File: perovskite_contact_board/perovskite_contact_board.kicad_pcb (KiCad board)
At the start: 4 copper layers, 57 x 52.2 mm, 15 parts, among them J1 Conn_2x3, J2 Conn_2x3, J3 Conn_2x3, J4 Conn_2x3, J5 Conn2x3, J6 Conn_2x3, U1 Perovskite_CP_6_Cell, U2 Perovskite_CP_6_Cell, U3 Perovskite_CP_6_Cell, U4 MCP9808_MSOP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

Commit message: pushing changes from Monday meeting
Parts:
- U4, U5, U6: moved to B.Cu
- moved U4 2.75 mm to (184.6, 81.7)
- moved R4 0.20 mm to (199.6, 78.0)
- turned U5 to 180 degrees
- turned U6 to 180 degrees
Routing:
- net CP: track 184.7 -> 0.00 mm, vias 3 -> 0
- net Vdd: track 116.8 -> 0.00 mm, vias 4 -> 0
- net GND: track 115.5 -> 0.00 mm, vias 3 -> 0
- net SCL: track 95.3 -> 0.30 mm
- net SDA: track 86.4 -> 0.00 mm, vias 4 -> 0
- net 16: track 35.4 -> 0.00 mm, vias 1 -> 0
- net 17: track 24.7 -> 0.00 mm, vias 1 -> 0
- net 18: track 23.8 -> 0.00 mm, vias 1 -> 0
- net 4: track 22.7 -> 0.00 mm, vias 1 -> 0
- net 7: track 22.6 -> 0.00 mm, vias 1 -> 0
- net 2: track 22.4 -> 0.00 mm, vias 1 -> 0
- net 5: track 22.2 -> 0.00 mm, vias 2 -> 0
- net 3: track 21.3 -> 0.00 mm, vias 1 -> 0
- net 12: track 20.2 -> 0.00 mm, vias 1 -> 0
- net 10: track 19.0 -> 0.00 mm, vias 1 -> 0
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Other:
- copper layers 4 -> 2
- rule trace_min: 0.2 -> 0.1524
- rule via_min_drill: 0.3 -> 0.254
- rule via_min_size: 0.4 -> 0.508

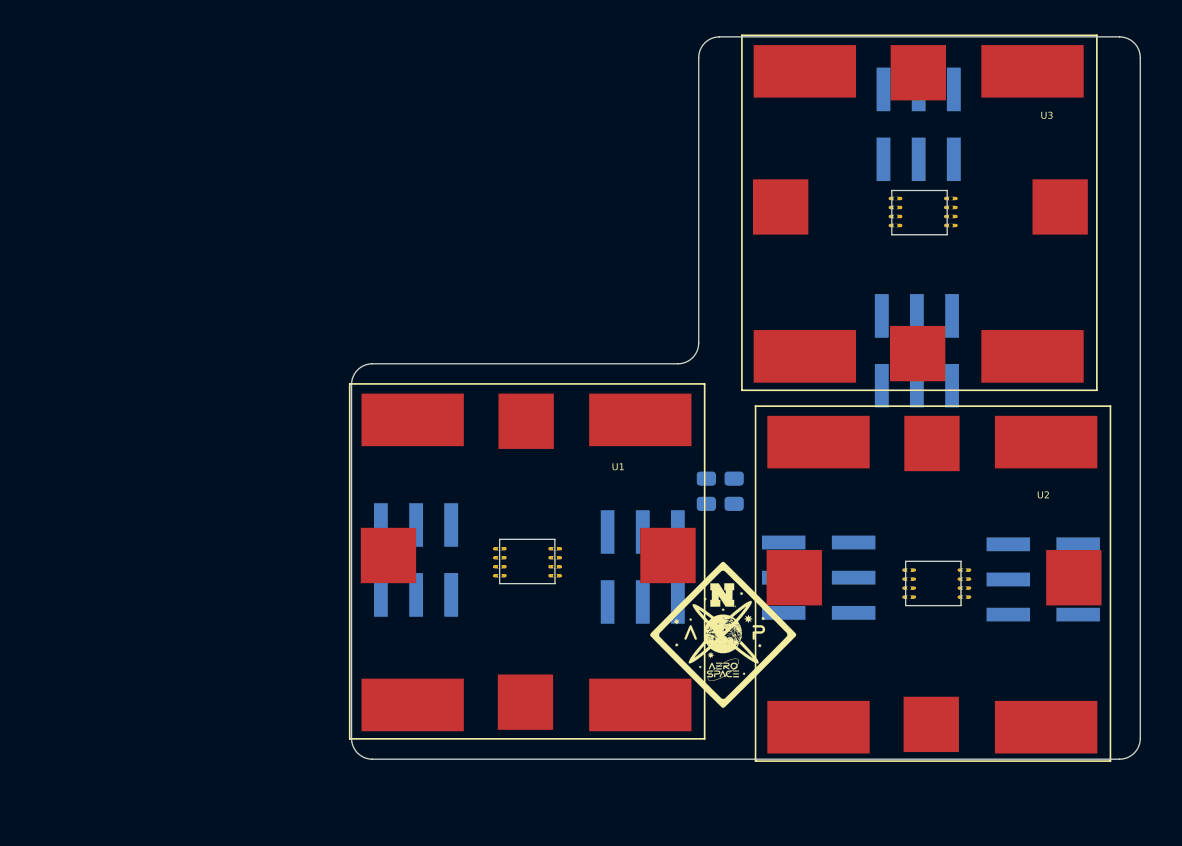
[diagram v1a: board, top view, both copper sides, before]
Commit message: Switched to 0603 package, no longer castillated holes used for the mcp9804, all traces on back layer
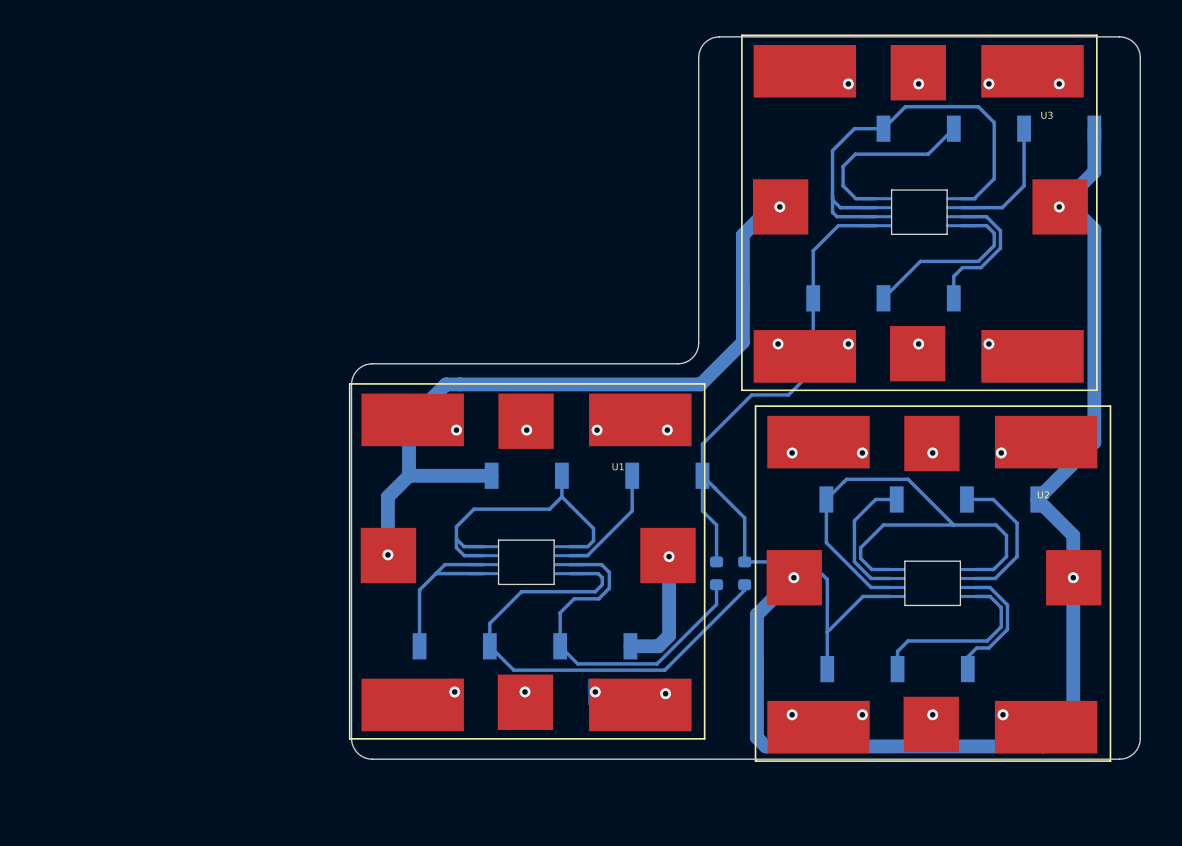
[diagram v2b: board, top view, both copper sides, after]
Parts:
- removed G***: LOGO, Logo:Smaller
- J1, J2, J3, J4, J6: value Conn_2x3 -> Conn_01x08; footprint Connector_PinHeader_2.54mm:PinHeader_2x03_P2.54mm_Vertical_SMD -> Connector_PinSocket_2.54mm:PinSocket_1x08_P2.54mm_Vertical_SMD_Pin1Left
- J5: value Conn2x3 -> Conn_01x08; footprint Connector_PinHeader_2.54mm:PinHeader_2x03_P2.54mm_Vertical_SMD -> Connector_PinSocket_2.54mm:PinSocket_1x08_P2.54mm_Vertical_SMD_Pin1Left
- R1, R4: footprint Resistor_SMD:R_0805_2012Metric -> Resistor_SMD:R_0603_1608Metric
- U4, U5, U6: footprint MCP9804Castillated:CastillatedMCP9804 -> MCP9804_Custom:MCP9804_With_Hole
- moved J3 14.3 mm to (210.2, 92.5), turned to 90 degrees
- moved J1 14.1 mm to (188.5, 75.2), turned to 90 degrees
- moved J2 10.3 mm to (185.8, 90.8), turned to 270 degrees
- moved J4 10.1 mm to (212.7, 76.9), turned to 90 degrees
- moved R4 5.98 mm to (200.4, 83.9)
- moved R1 5.98 mm to (198.4, 83.9)
- moved J6 4.26 mm to (209.2, 65.7)
- moved J5 4.04 mm to (216.8, 50.1), turned to 90 degrees
- moved U6 1.43 mm to (213.0, 57.8), turned to 0 degrees
- moved U5 1.37 mm to (214.0, 84.6), turned to 0 degrees
- moved U4 1.25 mm to (184.7, 82.9), turned to 0 degrees
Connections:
- J1 pad 1: 1 -> +5V
- J1 pad 2: 2 -> CELL_3
- J1 pad 3: 3 -> ALERT1
- J1 pad 4: 4 -> CELL_3
- J1 pad 5: 5 -> GND
- J1 pad 6: 6 -> CELL_2
- J2 pad 1: CP -> +5V
- J2 pad 2: SDA -> CELL_6
- J2 pad 3: SCL -> SDA
- J2 pad 4: Vdd -> CELL_5
- J2 pad 5: Alert1 -> SCL
- J2 pad 6: GND -> CELL_4
- J3 pad 1: 7 -> CELL_10
- J3 pad 2: 8 -> SCL
- J3 pad 3: 9 -> CELL_11
- J3 pad 4: 10 -> SDA
- J3 pad 5: 11 -> CELL_12
- J3 pad 6: 12 -> +5V
- J4 pad 2: SDA -> CELL_9
- J4 pad 3: SCL -> ALERT2
- J4 pad 4: Vdd -> CELL_8
- J4 pad 5: Alert2 -> +5V
- J4 pad 6: GND -> CELL_7
- J5 pad 1: 13 -> CP
- J5 pad 2: 14 -> CELL_15
- J5 pad 3: 15 -> ALERT3
- J5 pad 4: 16 -> CELL_15
- J5 pad 5: 17 -> +5V
- J5 pad 6: 18 -> CELL_14
- J6 pad 1: CP -> CELL_16
- J6 pad 2: SDA -> SCL
- J6 pad 3: SCL -> CELL_17
- J6 pad 4: Vdd -> SDA
- J6 pad 5: Alert3 -> CELL_18
- J6 pad 6: GND -> +5V
- R1 pad 1: Vdd -> +5V
- R4 pad 1: Vdd -> +5V
- U1 pad 1: 1 -> CELL_1
- U1 pad 2: 2 -> CELL_2
- U1 pad 3: 3 -> CELL_3
- U1 pad 4: 4 -> CELL_4
- U1 pad 5: 5 -> CELL_5
- U1 pad 6: 6 -> CELL_6
- U2 pad 1: 7 -> CELL_7
- U2 pad 2: 8 -> CELL_8
- U2 pad 3: 9 -> CELL_9
- U2 pad 4: 10 -> CELL_10
- U2 pad 5: 11 -> CELL_11
- U2 pad 6: 12 -> CELL_12
- U3 pad 1: 13 -> CELL_13
- U3 pad 2: 14 -> CELL_14
- U3 pad 3: 15 -> CELL_15
- U3 pad 4: 16 -> CELL_16
- U3 pad 5: 17 -> CELL_17
- U3 pad 6: 18 -> CELL_18
- U4 pad 3: Alert1 -> ALERT1
- U4 pad 7: Vdd -> +5V
- U4 pad 8: Vdd -> +5V
- U5 pad 3: Alert2 -> ALERT2
- U5 pad 6: Vdd -> +5V
- U5 pad 8: Vdd -> +5V
- U6 pad 3: Alert3 -> ALERT3
- U6 pad 5: Vdd -> +5V
- U6 pad 8: Vdd -> +5V
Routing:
- net CP: track 0.00 -> 147.4 mm, vias 0 -> 6
- net +5V: track 0.00 -> 95.0 mm
- net GND: track 0.00 -> 92.9 mm
- net SDA: track 0.00 -> 62.0 mm
- net SCL: track 0.30 -> 45.4 mm
- net ALERT2: track 0.00 -> 10.4 mm
- net ALERT3: track 0.00 -> 9.30 mm
- net ALERT1: track 0.00 -> 8.40 mm
- net CELL_9: vias 0 -> 1
- net CELL_8: vias 0 -> 1
- net CELL_7: vias 0 -> 2
- net CELL_6: vias 0 -> 1
- net CELL_5: vias 0 -> 1
- net CELL_4: vias 0 -> 2
- net CELL_3: vias 0 -> 2
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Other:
- outline, holes or cut-outs redrawn

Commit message: Contact board update with 2.54 spacing
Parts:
- moved R4 21.3 mm to (179.5, 87.6), turned to 0 degrees
- moved R1 19.7 mm to (179.5, 89.4), turned to 180 degrees
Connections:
- J5 pad 5: +5V -> GND
- J5 pad 7: GND -> +5V
- R1 pad 1: +5V -> SCL
- R1 pad 2: SCL -> +5V
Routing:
- net CP: track 147.4 -> 50.4 mm
- net +5V: track 95.0 -> 66.8 mm
- net SDA: track 62.0 -> 37.7 mm
- net SCL: track 45.4 -> 38.2 mm
- net GND: track 92.9 -> 88.6 mm
- added copper zone on B.Cu, net +5V
- added copper zone on B.Cu, net GND

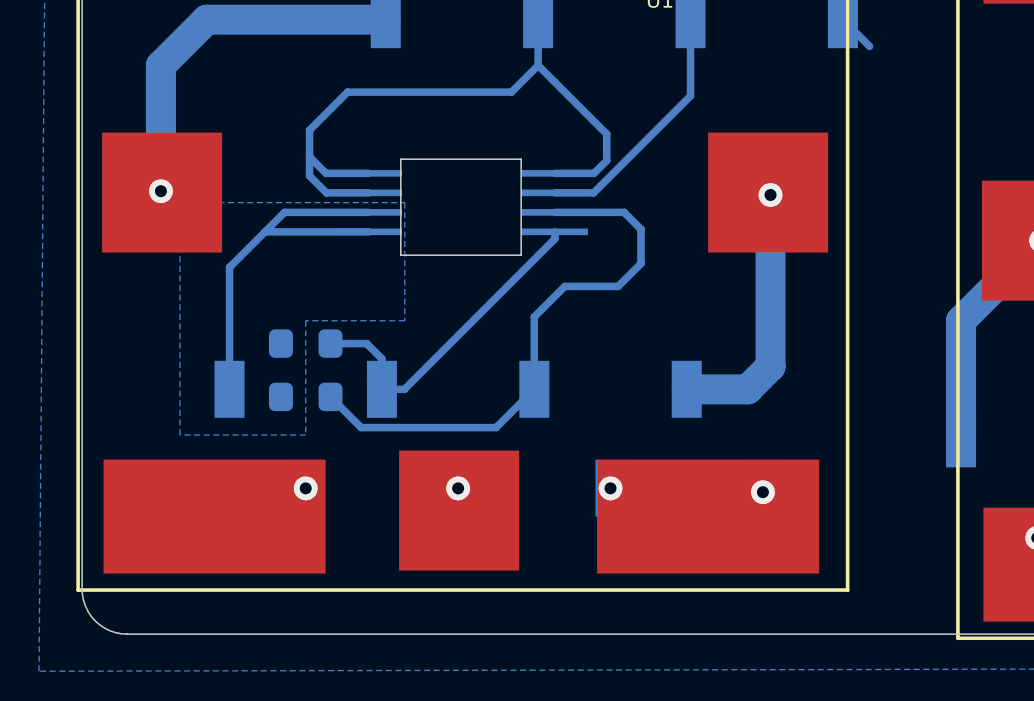
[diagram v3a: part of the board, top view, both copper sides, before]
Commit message: moved headers to fit connection to routing board and switch symbols to proper form
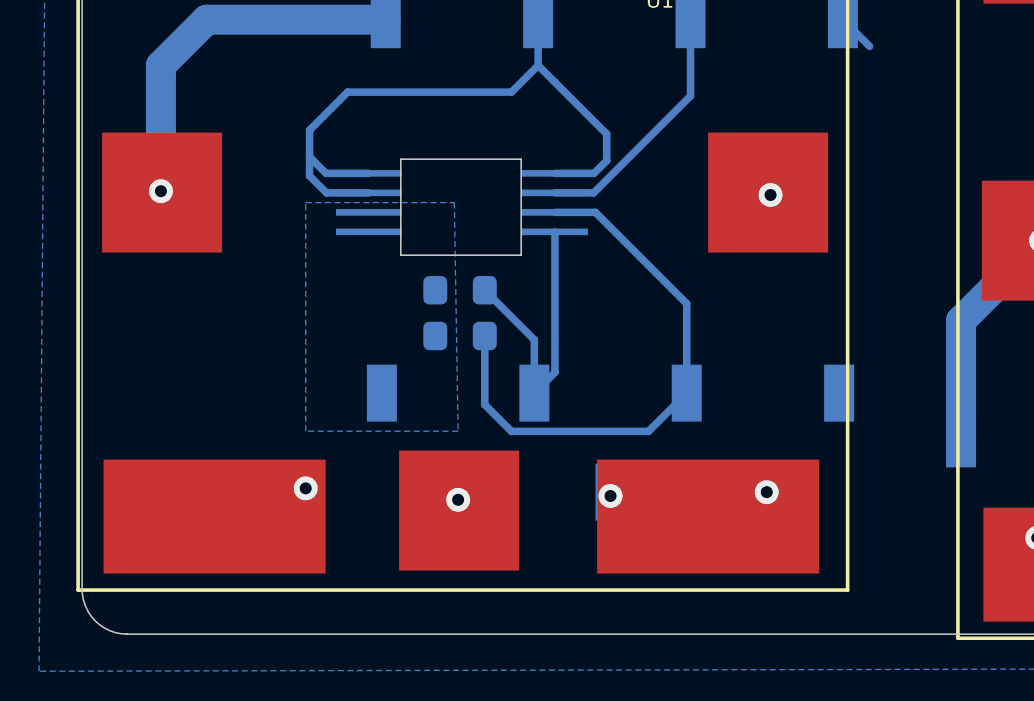
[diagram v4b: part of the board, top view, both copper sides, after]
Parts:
- J2: footprint Connector_PinSocket_2.54mm:PinSocket_1x08_P2.54mm_Vertical_SMD_Pin1Left -> Connector_PinSocket_2.54mm:PinSocket_1x08_P2.54mm_Vertical_SMD_Pin1Right
- moved R1 5.53 mm to (184.6, 87.4)
- moved R4 5.44 mm to (184.6, 85.9)
- moved J2 2.54 mm to (188.3, 90.9), turned to 90 degrees
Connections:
- J1 pad 1: +5V -> VDD
- J2 pad 1: +5V -> GND
- J2 pad 2: CELL_6 -> CELL_4
- J2 pad 3: SDA -> SCL
- J2 pad 4: CELL_5 -> CELL_4
- J2 pad 5: SCL -> SDA
- J2 pad 6: CELL_4 -> CELL_5
- J2 pad 7: CP -> VDD
- J2 pad 8: CELL_4 -> CELL_6
- J3 pad 6: +5V -> VDD
- J4 pad 5: +5V -> VDD
- J5 pad 7: +5V -> VDD
- J6 pad 6: +5V -> VDD
- U4 pad 7: +5V -> VDD
- U4 pad 8: +5V -> VDD
- U5 pad 6: +5V -> VDD
- U5 pad 8: +5V -> VDD
- U6 pad 5: +5V -> VDD
- U6 pad 8: +5V -> VDD
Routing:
- net +5V: track 66.8 -> 0.00 mm
- net VDD: track 0.00 -> 53.8 mm
- net CP: track 50.4 -> 41.5 mm
- net SDA: track 37.7 -> 35.9 mm

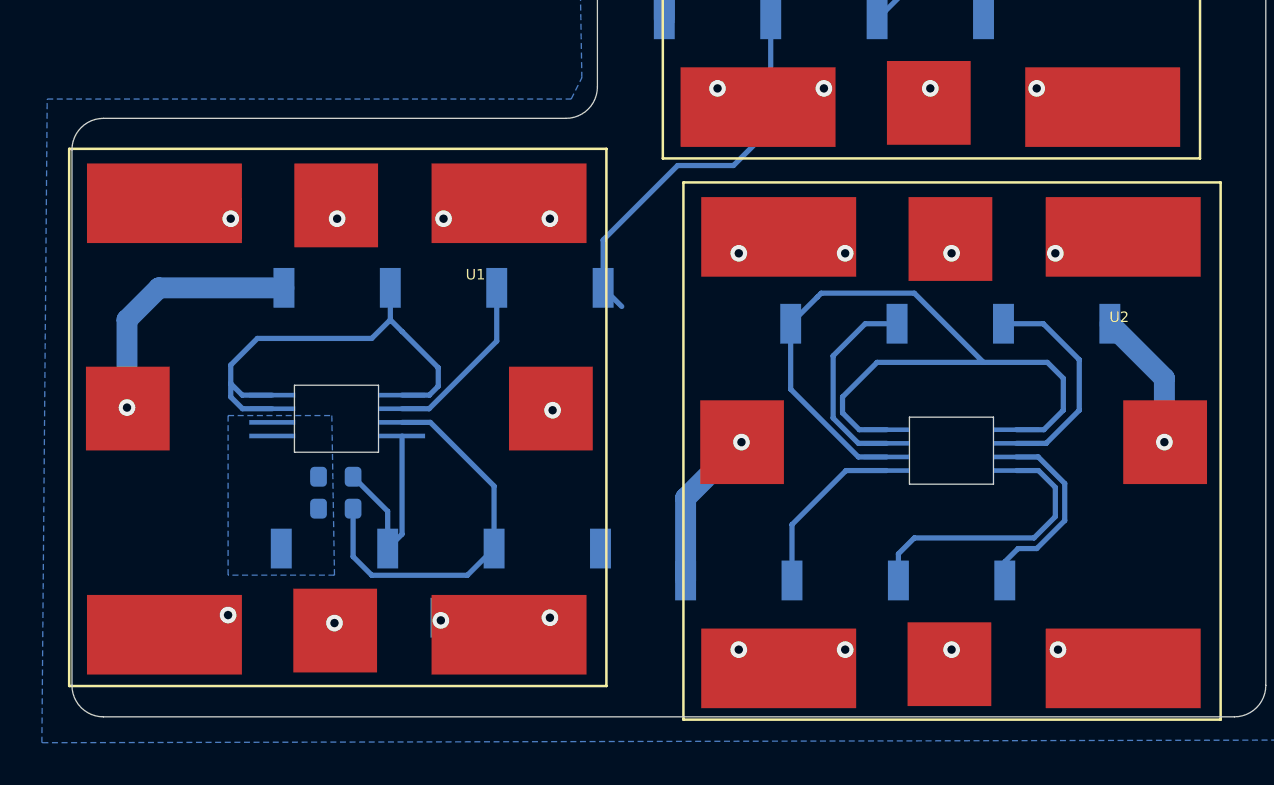
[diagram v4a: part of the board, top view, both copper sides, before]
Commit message: new headers added and spacing fixed to allow for 26 pin connector
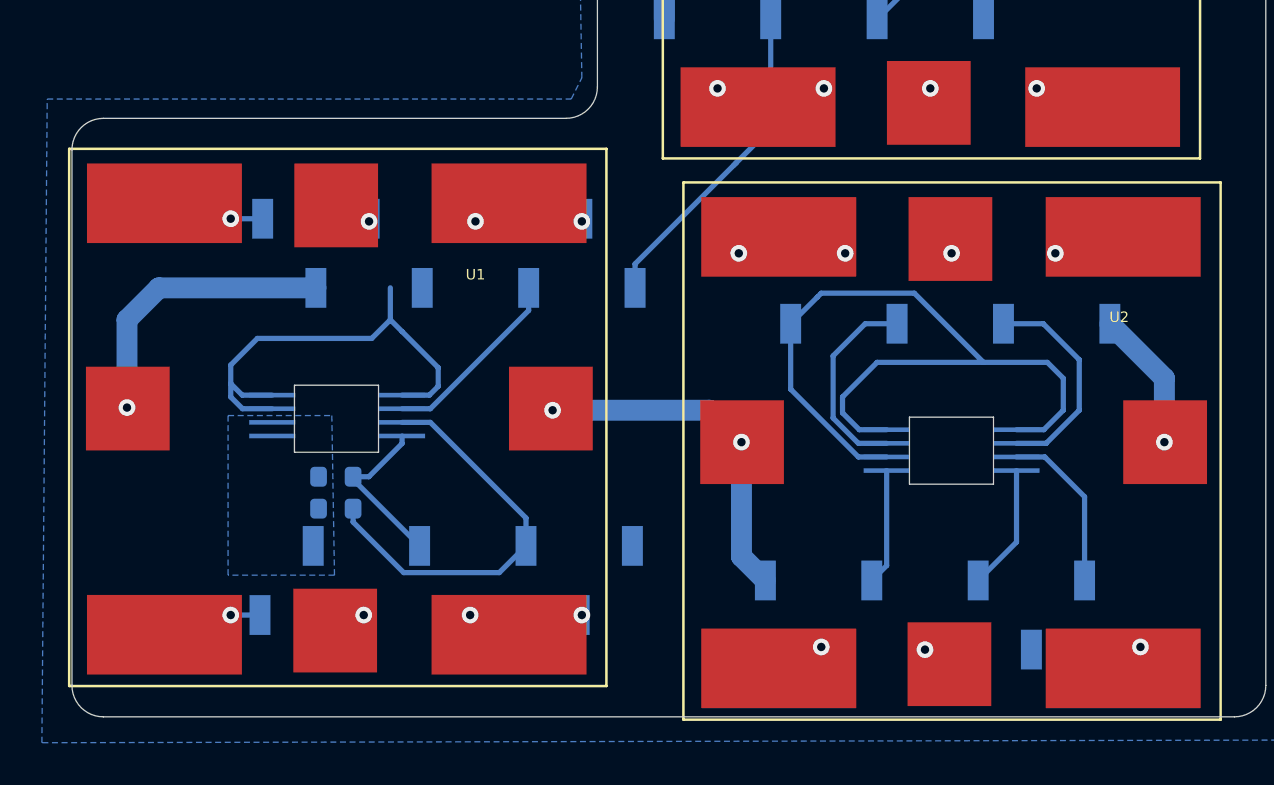
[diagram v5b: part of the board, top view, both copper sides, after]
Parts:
- moved J3 3.81 mm to (214.0, 92.5)
- moved J2 1.53 mm to (189.9, 90.8)
- moved J1 1.52 mm to (190.0, 75.2)
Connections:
- J3 pad 3: CELL_11 -> (no net)
- J3 pad 5: CELL_12 -> CELL_11
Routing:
- net CP: track 41.5 -> 52.1 mm
- net SDA: track 35.9 -> 27.0 mm
- net VDD: track 53.8 -> 47.8 mm
- net CELL_1: track 0.00 -> 1.52 mm
- net CELL_6: track 0.00 -> 1.40 mm
- net ALERT1: track 8.40 -> 9.07 mm
- net CELL_12: vias 2 -> 1
